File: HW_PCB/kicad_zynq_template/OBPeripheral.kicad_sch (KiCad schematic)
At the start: 44 parts, among them IC1 Atmel AVR ATtiny10, J2 MMC SD Socket, J3 U.FL-R-SMT-1, J4 SCHD3A0100, SW1 4pin button, U5 TiWi-uB2, U6 ATSHA204A-STUCZ-T

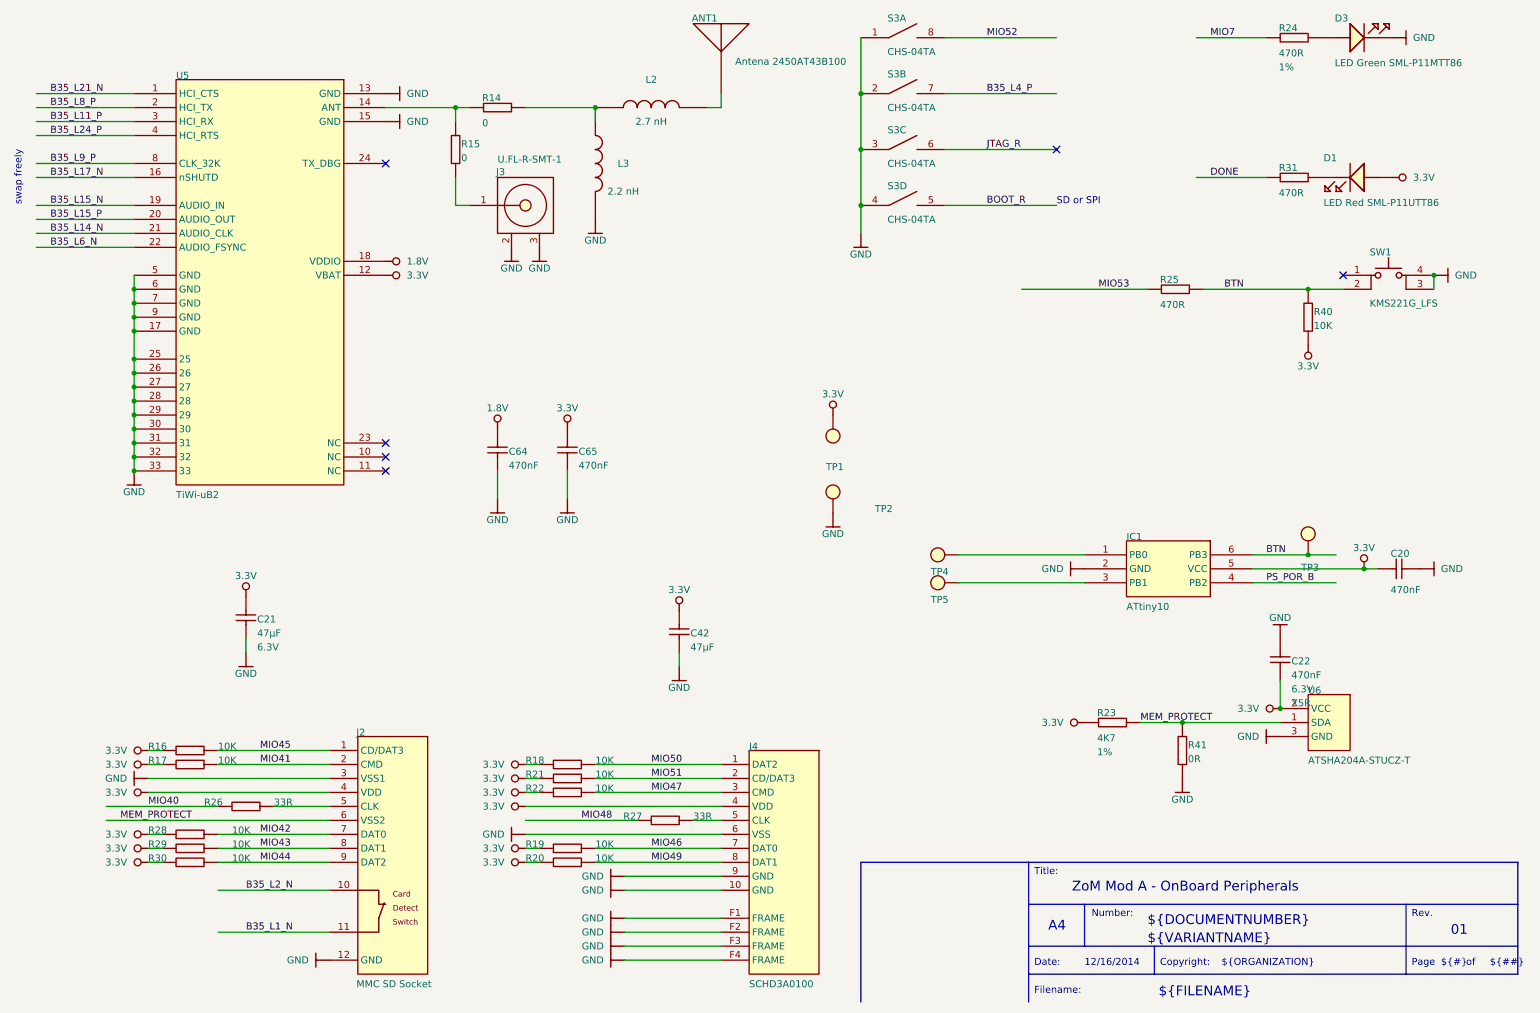
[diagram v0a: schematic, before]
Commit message: pcbs tidied up
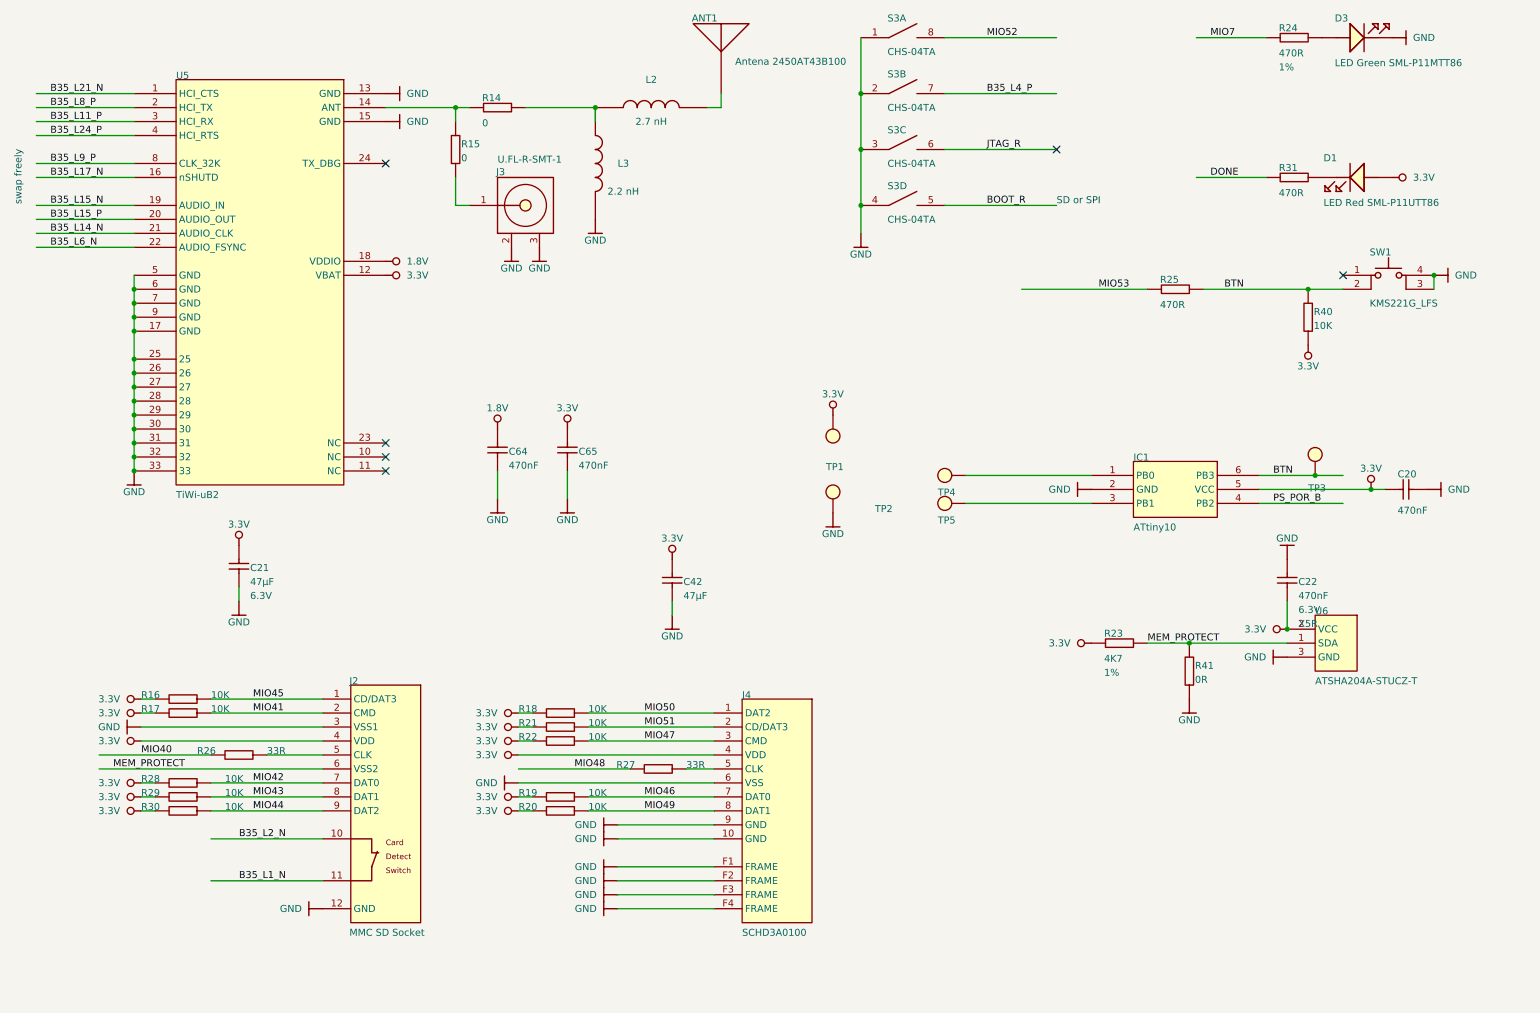
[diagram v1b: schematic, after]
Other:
- note removed: "${##}"
- note removed: "${#}"
- note removed: "${DOCUMENTNUMBER}"
- note removed: "${FILENAME}"
- note removed: "${ISSUE_DATE}"
- note removed: "${ORGANIZATION}"
- note removed: "${REVISION}"
- note removed: "${TITLE}"
- note removed: "${VARIANTNAME}"
- note removed: "A4"
- note removed: "Copyright:"
- note removed: "Date:"
- note removed: "Filename:"
- note removed: "Number:"
- note removed: "Page"
- note removed: "Rev."
- note removed: "Title:"
- note removed: "of"
- moved on the sheet: C20, C21, C22, C42, IC1, J2, J4, R16, R17, R18, R19, R20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
